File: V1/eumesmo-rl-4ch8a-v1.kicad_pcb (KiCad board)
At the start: 2 copper layers, 53 x 67.8 mm, 25 parts, among them J1 250-202, J2 250-204, J3 DB142V-5.08-4P, J4 DB142V-5.08-4P, K1 G5Q-1A4-DC24V, K2 G5Q-1A4-DC24V, K3 G5Q-1A4-DC24V, K4 G5Q-1A4-DC24V

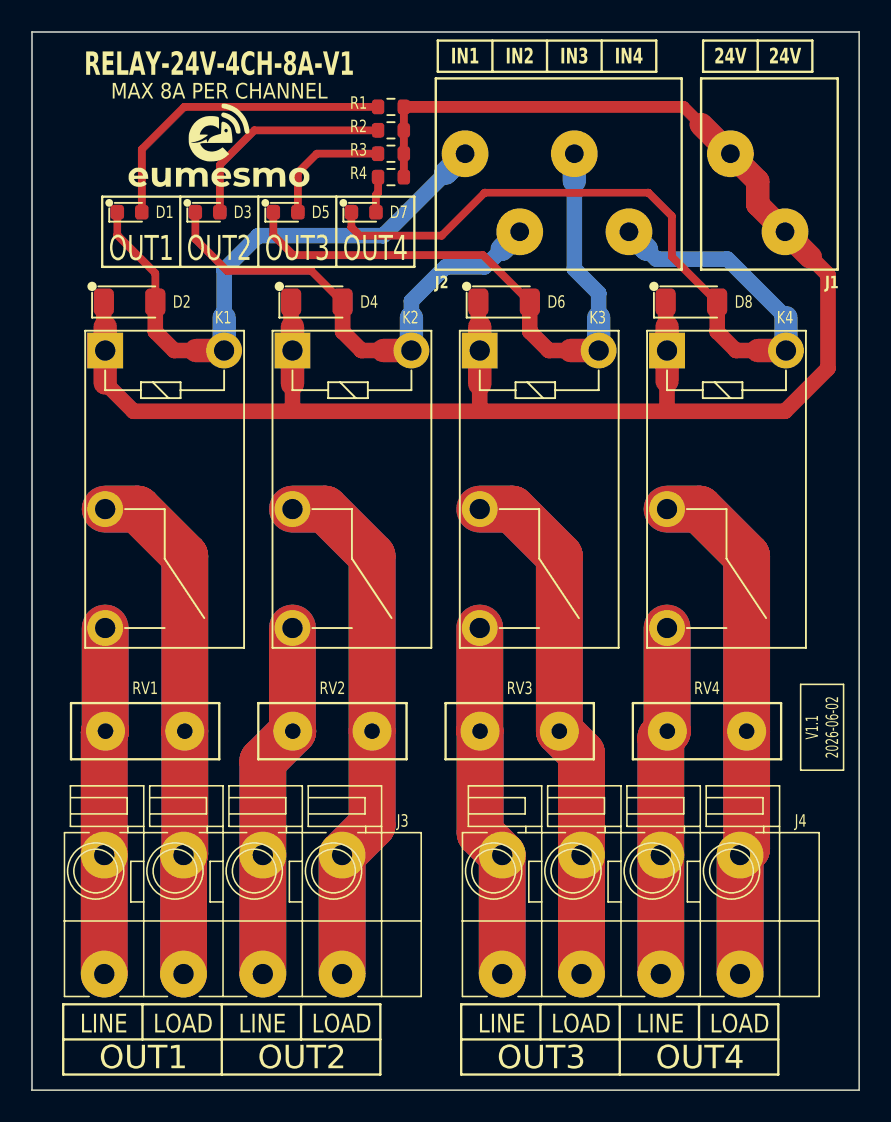
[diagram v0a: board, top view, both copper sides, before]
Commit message: Updated version numbers.
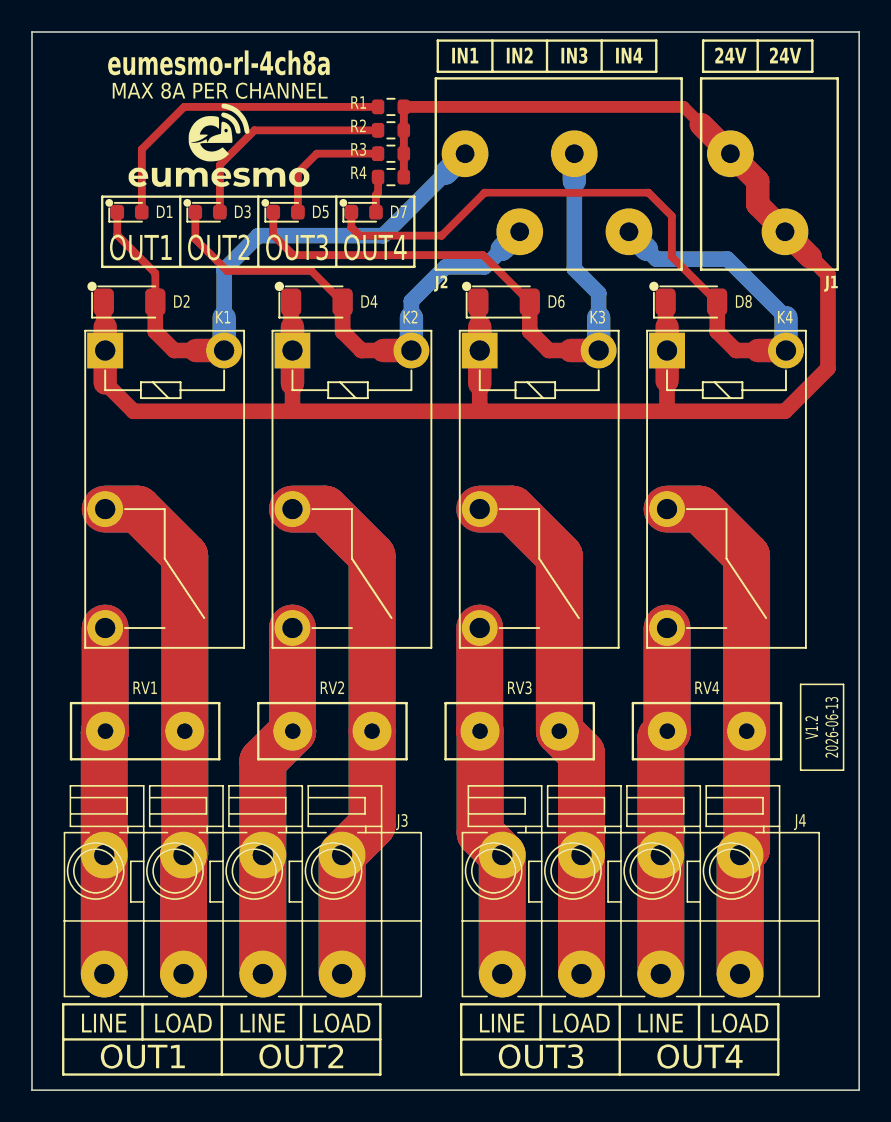
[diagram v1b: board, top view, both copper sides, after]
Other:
- board text added: "V1.2 2026-06-13"
- board text added: "eumesmo-rl-4ch8a"
- board text removed: "RELAY-24V-4CH-8A-V1"
- board text removed: "V1.1 2026-06-02"
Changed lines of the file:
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@@
 	(paper "A4")
 	(title_block
-		(title "4x 24V 8A Relay Module")
-		(date "2026-06-02")
-		(rev "V1.1")
+		(title "eumesmo 4x 24V 8A Relay Module")
+		(date "2026-06-13")
+		(rev "V1.2")
 	)
 	(layers
@@
 		(property ki_fp_filters "Relay*SPST*Omron*G5PZ*")
 		(sheetname "/")
-		(sheetfile "relay-24v-4ch-8a-v1.kicad_sch")
+		(sheetfile "eumesmo-rl-4ch8a-v1.kicad_sch")
 		(units
 			(unit
@@
 		(property ki_fp_filters "R_*")
 		(sheetname "/")
-		(sheetfile "relay-24v-4ch-8a-v1.kicad_sch")
+		(sheetfile "eumesmo-rl-4ch8a-v1.kicad_sch")
 		(units
 			(unit
@@
 		(property ki_fp_filters "TO-???* *_Diode_* *SingleDiode* D_*")
 		(sheetname "/")
-		(sheetfile "relay-24v-4ch-8a-v1.kicad_sch")
+		(sheetfile "eumesmo-rl-4ch8a-v1.kicad_sch")
 		(units
 			(unit
@@
 		(property ki_fp_filters "Relay*SPST*Omron*G5PZ*")
 		(sheetname "/")
-		(sheetfile "relay-24v-4ch-8a-v1.kicad_sch")
+		(sheetfile "eumesmo-rl-4ch8a-v1.kicad_sch")
 		(units
 			(unit
@@
 		(property ki_fp_filters "LED* LED_SMD:* LED_THT:*")
 		(sheetname "/")
-		(sheetfile "relay-24v-4ch-8a-v1.kicad_sch")
+		(sheetfile "eumesmo-rl-4ch8a-v1.kicad_sch")
 		(units
 			(unit
@@
 		(property ki_fp_filters "R_*")
 		(sheetname "/")
-		(sheetfile "relay-24v-4ch-8a-v1.kicad_sch")
+		(sheetfile "eumesmo-rl-4ch8a-v1.kicad_sch")
 		(units
 			(unit
@@
 		(property ki_fp_filters "LED* LED_SMD:* LED_THT:*")
 		(sheetname "/")
-		(sheetfile "relay-24v-4ch-8a-v1.kicad_sch")
+		(sheetfile "eumesmo-rl-4ch8a-v1.kicad_sch")
 		(units
 			(unit
@@
 		(property ki_fp_filters "R_*")
 		(sheetname "/")
-		(sheetfile "relay-24v-4ch-8a-v1.kicad_sch")
+		(sheetfile "eumesmo-rl-4ch8a-v1.kicad_sch")
 		(units
 			(unit
@@
 		(property ki_fp_filters "TO-???* *_Diode_* *SingleDiode* D_*")
 		(sheetname "/")
-		(sheetfile "relay-24v-4ch-8a-v1.kicad_sch")
+		(sheetfile "eumesmo-rl-4ch8a-v1.kicad_sch")
 		(units
 			(unit
@@
 		(property ki_fp_filters "RV_* Varistor*")
 		(sheetname "/")
-		(sheetfile "relay-24v-4ch-8a-v1.kicad_sch")
+		(sheetfile "eumesmo-rl-4ch8a-v1.kicad_sch")
 		(units
 			(unit
@@
 		(property ki_fp_filters "TO-???* *_Diode_* *SingleDiode* D_*")
 		(sheetname "/")
-		(sheetfile "relay-24v-4ch-8a-v1.kicad_sch")
+		(sheetfile "eumesmo-rl-4ch8a-v1.kicad_sch")
 		(units
 			(unit
@@
 		(property ki_fp_filters "LED* LED_SMD:* LED_THT:*")
 		(sheetname "/")
-		(sheetfile "relay-24v-4ch-8a-v1.kicad_sch")
+		(sheetfile "eumesmo-rl-4ch8a-v1.kicad_sch")
 		(units
 			(unit
@@
 		(property ki_fp_filters "RV_* Varistor*")
 		(sheetname "/")
-		(sheetfile "relay-24v-4ch-8a-v1.kicad_sch")
+		(sheetfile "eumesmo-rl-4ch8a-v1.kicad_sch")
 		(units
 			(unit
@@
 		(property ki_fp_filters "RV_* Varistor*")
 		(sheetname "/")
-		(sheetfile "relay-24v-4ch-8a-v1.kicad_sch")
+		(sheetfile "eumesmo-rl-4ch8a-v1.kicad_sch")
 		(units
 			(unit
@@
 		(property ki_fp_filters "Connector*:*_1x??_*")
 		(sheetname "/")
-		(sheetfile "relay-24v-4ch-8a-v1.kicad_sch")
+		(sheetfile "eumesmo-rl-4ch8a-v1.kicad_sch")
 		(units
 			(unit
@@
 		(property ki_fp_filters "TO-???* *_Diode_* *SingleDiode* D_*")
 		(sheetname "/")
-		(sheetfile "relay-24v-4ch-8a-v1.kicad_sch")
+		(sheetfile "eumesmo-rl-4ch8a-v1.kicad_sch")
 		(units
 			(unit
@@
 		(property ki_fp_filters "Connector*:*_1x??_*")
 		(sheetname "/")
-		(sheetfile "relay-24v-4ch-8a-v1.kicad_sch")
+		(sheetfile "eumesmo-rl-4ch8a-v1.kicad_sch")
 		(units
 			(unit
@@
 		(property ki_fp_filters "Connector*:*_1x??_*")
 		(sheetname "/")
-		(sheetfile "relay-24v-4ch-8a-v1.kicad_sch")
+		(sheetfile "eumesmo-rl-4ch8a-v1.kicad_sch")
 		(units
 			(unit
@@
 		(property ki_fp_filters "RV_* Varistor*")
 		(sheetname "/")
-		(sheetfile "relay-24v-4ch-8a-v1.kicad_sch")
+		(sheetfile "eumesmo-rl-4ch8a-v1.kicad_sch")
 		(units
 			(unit
@@
 		(property ki_fp_filters "R_*")
 		(sheetname "/")
-		(sheetfile "relay-24v-4ch-8a-v1.kicad_sch")
+		(sheetfile "eumesmo-rl-4ch8a-v1.kicad_sch")
 		(units
 			(unit
@@
 		(property ki_fp_filters "Relay*SPST*Omron*G5PZ*")
 		(sheetname "/")
-		(sheetfile "relay-24v-4ch-8a-v1.kicad_sch")
+		(sheetfile "eumesmo-rl-4ch8a-v1.kicad_sch")
 		(units
 			(unit
@@
 		(property ki_fp_filters "Relay*SPST*Omron*G5PZ*")
 		(sheetname "/")
-		(sheetfile "relay-24v-4ch-8a-v1.kicad_sch")
+		(sheetfile "eumesmo-rl-4ch8a-v1.kicad_sch")
 		(units
 			(unit
@@
 		(property ki_fp_filters "LED* LED_SMD:* LED_THT:*")
 		(sheetname "/")
-		(sheetfile "relay-24v-4ch-8a-v1.kicad_sch")
+		(sheetfile "eumesmo-rl-4ch8a-v1.kicad_sch")
 		(units
 			(unit
@@
 		(property ki_fp_filters "Connector*:*_1x??_*")
 		(sheetname "/")
-		(sheetfile "relay-24v-4ch-8a-v1.kicad_sch")
+		(sheetfile "eumesmo-rl-4ch8a-v1.kicad_sch")
 		(units
 			(unit
@@
 		(layer "Edge.Cuts")
 	)
-	(gr_text "V1.1\n2026-06-02"
+	(gr_text "V1.2\n2026-06-13"
 		(at 176.75 106.75 90)
 		(layer "F.SilkS")
@@
 		)
 	)
-	(gr_text "RELAY-24V-4CH-8A-V1"
+	(gr_text "eumesmo-rl-4ch8a"
 		(at 137 64.25 0)
 		(layer "F.SilkS")
@@
 			(font
 				(size 1.5 1)
-				(thickness 0.25)
+				(thickness 0.2)
 				(bold yes)
 			)

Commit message: Release V1.2.0
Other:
- board text added: "V1.2 2026-06-17"
- board text removed: "V1.2 2026-06-13"
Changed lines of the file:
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@@
 	(title_block
 		(title "eumesmo 4x 24V 8A Relay Module")
-		(date "2026-06-13")
+		(date "2026-06-17")
 		(rev "V1.2")
 	)
@@
 	)
 	(gr_rect
-		(start 174.25 104)
-		(end 177 109.5)
+		(start 175.5 102.25)
+		(end 177 109.75)
 		(stroke
 			(width 0.1)
@@
 		(layer "Edge.Cuts")
 	)
-	(gr_text "V1.2\n2026-06-13"
-		(at 176.75 106.75 90)
+	(gr_text "V1.2 2026-06-17"
+		(at 176.25 106 90)
 		(layer "F.SilkS")
 		(effects
@@
 				(thickness 0.1)
 			)
-			(justify bottom)
 		)
 	)
